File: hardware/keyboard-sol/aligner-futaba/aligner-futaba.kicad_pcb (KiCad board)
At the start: 2 copper layers, 386.1 x 117.7 mm, 96 parts, among them SW10 TAB: 1.25x, SW11 I, SW12 2, SW13 Zero, SW14 Q, SW15 O, SW16 3, SW17 Dash, SW18 W, SW19 P, SW20 4, SW21 Caret, SW22 E, SW23 AT, SW24 5, SW25 LT Bracket, SW26 R, SW27 Return: 1.5x, SW28 6, SW29 Backslash, SW30 T, SW31 Line Feed, SW32 7, SW33 RT Bracket, SW34 Y, SW35 Load, SW36 LT Ctrl, SW37 J, SW38 Upper Case: 1.5x, SW39 M, SW4 ESC: 1.75x, SW40 Shift Lock: 1.5x, SW41 K, SW42 LT Shift: 1.5x, SW43 Comma, SW44 A, SW45 L, SW46 Z, SW47 Period, SW48 S, SW49 Semicolon, SW5 8, SW50 X, SW51 Slash, SW52 D, SW53 Colon, SW54 C, SW55 RT Shift: 2x, SW56 F, SW57 DEL, SW58 V, SW59 Mode Select: 1.75x, SW6 BREAK, SW60 G, SW61 Repeat: 1.25x, SW62 B, SW63 H, SW64 RT Ctrl, SW65 N, SW66 Local, SW67 NP Dash, SW68 NP 4, SW69 NP Zero, SW7 U, SW70 Up Arrow, SW71 NP 7, SW72 NP 1, SW73 NP period, SW74 LT Arrow, SW75 NP asterisk, SW76 NP 5, SW77 NP plus, SW78 Spacebar, SW79 NP 8, SW8 1, SW80 NP 2, SW81 RT Arrow, SW82 NP divide, SW83 NP 6, SW84 Down Arrow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

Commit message: Moved mounting slots from keyboard PCB to aligners
- This allows the PCB to sink below the mounting brackets.  The aligner height can
be adjusted relative to the mounting brackets using spacers.

- changed futaba aligners to use cherry stabilizers.

- bumped rev number
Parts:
- removed the REF** at (318.1, 206.8)
- removed the REF** at (184.8, 206.8)
- SW55: footprint unikbd:Futaba-MD-4PCS-aligner -> unikbd:Futaba_2u_Cherry_aligner
- SW78: footprint unikbd:Futaba-MD-4PCS-aligner -> unikbd:Futaba_space_Cherry_aligner
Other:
- board size 386.1 x 117.7 mm -> 428.6 x 117.7 mm
- board text added: "SOL-20 Futaba MD-4PCS aligner Rev 1.1"
- board text removed: "SOL-20 Futaba MD-4PCS aligner Rev 1.0"

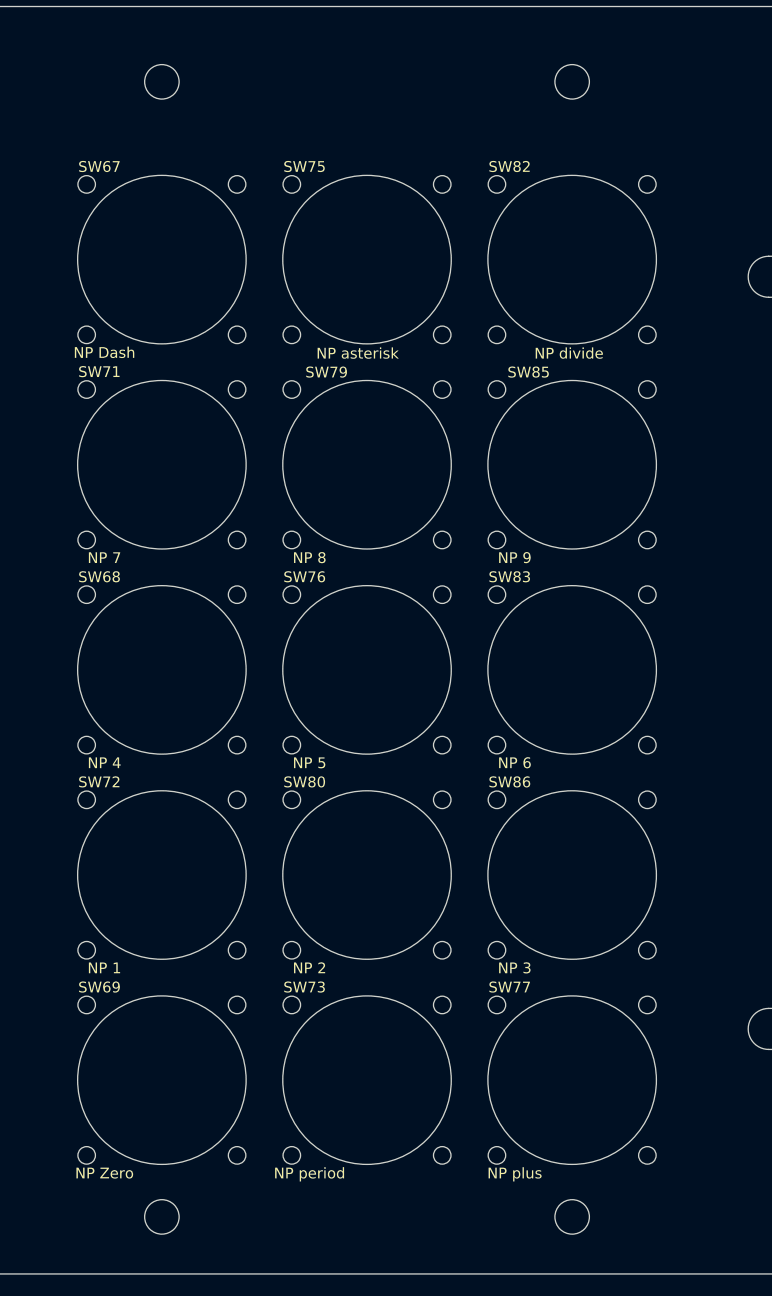
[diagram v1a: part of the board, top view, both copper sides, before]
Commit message: On aligners, moved numpad 0.1825" to the right.
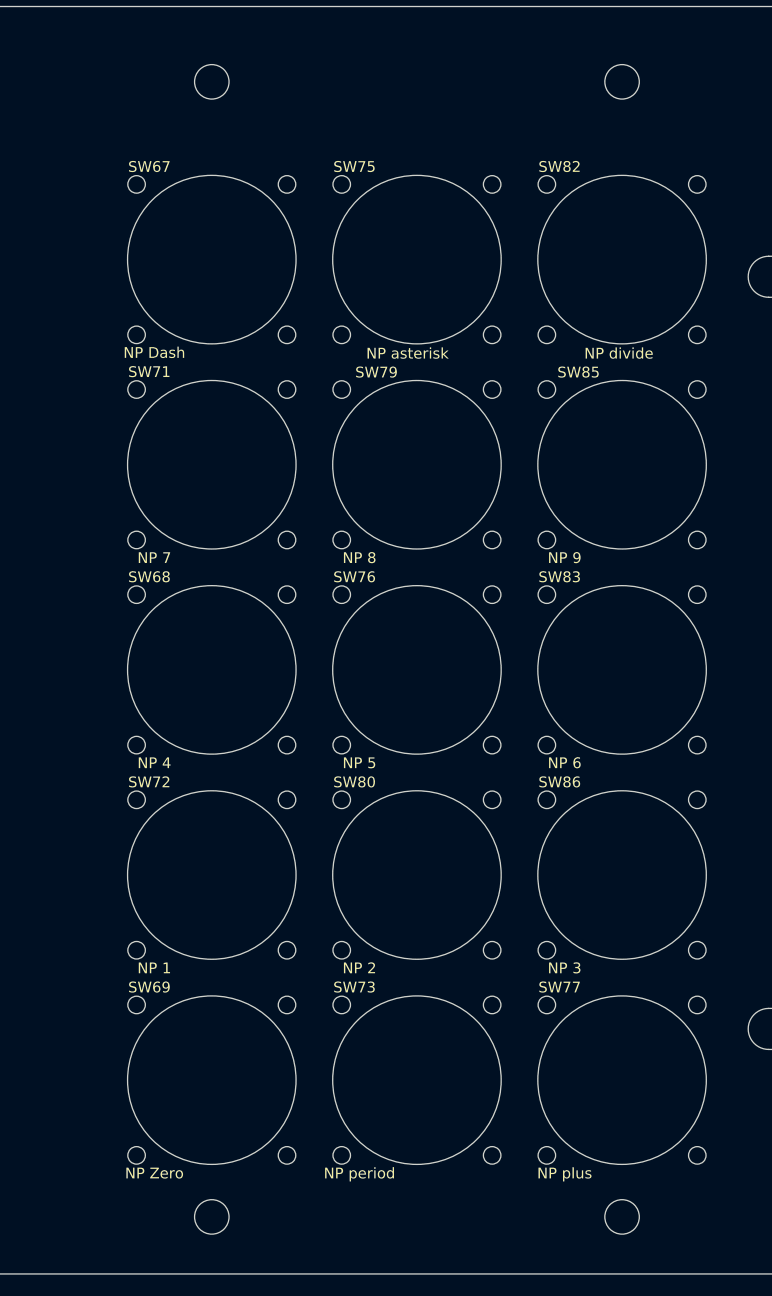
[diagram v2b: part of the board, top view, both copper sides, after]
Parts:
- removed the REF** at (432.4, 219.5)
- removed the REF** at (470.5, 219.5)
- removed the REF** at (470.5, 114.1)
- removed the REF** at (432.4, 114.1)
- added REF**: MountingHole_3.2mm_M3, MountingHole:MountingHole_3.2mm_M3, F.Cu at (437.1, 219.5)
- added REF**: MountingHole_3.2mm_M3, MountingHole:MountingHole_3.2mm_M3, F.Cu at (475.2, 219.5)
- added REF**: MountingHole_3.2mm_M3, MountingHole:MountingHole_3.2mm_M3, F.Cu at (475.2, 114.1)
- added REF**: MountingHole_3.2mm_M3, MountingHole:MountingHole_3.2mm_M3, F.Cu at (437.1, 114.1)
- moved SW73 4.64 mm to (456.1, 206.8)
- moved SW75 4.64 mm to (456.1, 130.6)
- moved SW76 4.64 mm to (456.1, 168.7)
- moved SW79 4.64 mm to (456.1, 149.6)
- moved SW80 4.64 mm to (456.1, 187.7)
- moved SW67 4.64 mm to (437.1, 130.6)
- moved SW68 4.64 mm to (437.1, 168.7)
- moved SW69 4.64 mm to (437.1, 206.8)
- moved SW71 4.64 mm to (437.1, 149.6)
- moved SW72 4.64 mm to (437.1, 187.7)
- moved SW77 4.64 mm to (475.2, 206.8)
- moved SW82 4.64 mm to (475.2, 130.6)
- moved SW83 4.64 mm to (475.2, 168.7)
- moved SW85 4.64 mm to (475.2, 149.6)
- moved SW86 4.64 mm to (475.2, 187.7)
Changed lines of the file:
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@@
   )
   (module unikbd:Futaba-MD-4PCS-aligner locked (layer F.Cu)
-    (at 451.47738 168.69156)
+    (at 456.11288 168.69156)
     (fp_text reference SW76 (at -5.7912 -8.6106) (layer F.SilkS)
       (effects (font (size 1 1) (thickness 0.15)))
@@
   )
   (module unikbd:Futaba-MD-4PCS-aligner locked (layer F.Cu)
-    (at 432.42738 168.69156)
+    (at 437.06288 168.69156)
     (fp_text reference SW68 (at -5.7912 -8.6106) (layer F.SilkS)
       (effects (font (size 1 1) (thickness 0.15)))
@@
   )
   (module unikbd:Futaba-MD-4PCS-aligner locked (layer F.Cu)
-    (at 470.52738 168.69156)
+    (at 475.16288 168.69156)
     (fp_text reference SW83 (at -5.7912 -8.6106) (layer F.SilkS)
       (effects (font (size 1 1) (thickness 0.15)))
@@
   )
   (module unikbd:Futaba-MD-4PCS-aligner locked (layer F.Cu)
-    (at 470.52738 149.64156)
+    (at 475.16288 149.64156)
     (fp_text reference SW85 (at -4.03098 -8.56996) (layer F.SilkS)
       (effects (font (size 1 1) (thickness 0.15)))
@@
   )
   (module unikbd:Futaba-MD-4PCS-aligner locked (layer F.Cu)
-    (at 470.52738 187.74156)
+    (at 475.16288 187.74156)
     (fp_text reference SW86 (at -5.7912 -8.6106) (layer F.SilkS)
       (effects (font (size 1 1) (thickness 0.15)))
@@
   )
   (module unikbd:Futaba-MD-4PCS-aligner locked (layer F.Cu)
-    (at 470.52738 130.59156)
+    (at 475.16288 130.59156)
     (fp_text reference SW82 (at -5.7912 -8.6106) (layer F.SilkS)
       (effects (font (size 1 1) (thickness 0.15)))
@@
   )
   (module unikbd:Futaba-MD-4PCS-aligner locked (layer F.Cu)
-    (at 451.47738 187.74156)
+    (at 456.11288 187.74156)
     (fp_text reference SW80 (at -5.7912 -8.6106) (layer F.SilkS)
       (effects (font (size 1 1) (thickness 0.15)))
@@
   )
   (module unikbd:Futaba-MD-4PCS-aligner locked (layer F.Cu)
-    (at 451.47738 149.64156)
+    (at 456.11288 149.64156)
     (fp_text reference SW79 (at -3.75158 -8.56996) (layer F.SilkS)
       (effects (font (size 1 1) (thickness 0.15)))
@@
   )
   (module unikbd:Futaba-MD-4PCS-aligner locked (layer F.Cu)
-    (at 470.52738 206.79156)
+    (at 475.16288 206.79156)
     (fp_text reference SW77 (at -5.7912 -8.6106) (layer F.SilkS)
       (effects (font (size 1 1) (thickness 0.15)))
@@
   )
   (module unikbd:Futaba-MD-4PCS-aligner locked (layer F.Cu)
-    (at 451.47738 130.59156)
+    (at 456.11288 130.59156)
     (fp_text reference SW75 (at -5.7912 -8.6106) (layer F.SilkS)
       (effects (font (size 1 1) (thickness 0.15)))
@@
   )
   (module unikbd:Futaba-MD-4PCS-aligner locked (layer F.Cu)
-    (at 451.47738 206.79156)
+    (at 456.11288 206.79156)
     (fp_text reference SW73 (at -5.7912 -8.6106) (layer F.SilkS)
       (effects (font (size 1 1) (thickness 0.15)))
@@
   )
   (module unikbd:Futaba-MD-4PCS-aligner locked (layer F.Cu)
-    (at 432.42738 187.74156)
+    (at 437.06288 187.74156)
     (fp_text reference SW72 (at -5.7912 -8.6106) (layer F.SilkS)
       (effects (font (size 1 1) (thickness 0.15)))
@@
   )
   (module unikbd:Futaba-MD-4PCS-aligner locked (layer F.Cu)
-    (at 432.42738 149.64156)
+    (at 437.06288 149.64156)
     (fp_text reference SW71 (at -5.7912 -8.6106) (layer F.SilkS)
       (effects (font (size 1 1) (thickness 0.15)))
@@
   )
   (module unikbd:Futaba-MD-4PCS-aligner locked (layer F.Cu)
-    (at 432.42738 206.79156)
+    (at 437.06288 206.79156)
     (fp_text reference SW69 (at -5.7912 -8.6106) (layer F.SilkS)
       (effects (font (size 1 1) (thickness 0.15)))
@@
   )
   (module unikbd:Futaba-MD-4PCS-aligner locked (layer F.Cu)
-    (at 432.42738 130.59156)
+    (at 437.06288 130.59156)
     (fp_text reference SW67 (at -5.7912 -8.6106) (layer F.SilkS)
       (effects (font (size 1 1) (thickness 0.15)))
@@
   )
   (module MountingHole:MountingHole_3.2mm_M3 locked (layer F.Cu)
-    (at 432.42738 219.49156)
+    (at 437.06288 219.49156)
     (descr "Mounting Hole 3.2mm, no annular, M3")
     (tags "mounting hole 3.2mm no annular m3")
@@
   )
   (module MountingHole:MountingHole_3.2mm_M3 locked (layer F.Cu)
-    (at 470.52738 219.49156)
+    (at 475.16288 219.49156)
     (descr "Mounting Hole 3.2mm, no annular, M3")
     (tags "mounting hole 3.2mm no annular m3")
@@
   )
   (module MountingHole:MountingHole_3.2mm_M3 locked (layer F.Cu)
-    (at 470.52738 114.08156)
+    (at 475.16288 114.08156)
     (descr "Mounting Hole 3.2mm, no annular, M3")
     (tags "mounting hole 3.2mm no annular m3")
@@
   )
   (module MountingHole:MountingHole_3.2mm_M3 locked (layer F.Cu)
-    (at 432.42738 114.08156)
+    (at 437.06288 114.08156)
     (descr "Mounting Hole 3.2mm, no annular, M3")
     (tags "mounting hole 3.2mm no annular m3")

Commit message: Adjsut mounting slots and alignment of mounting holes.
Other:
- outline, holes or cut-outs redrawn
- board text added: "SOL-20 Futaba MD-4PCS aligner Rev 1.4"
- board text removed: "SOL-20 Futaba MD-4PCS aligner Rev 1.1"
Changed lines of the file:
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@@
   (gr_circle (center 102.16388 187.74156) (end 105.38968 187.74156) (layer Edge.Cuts) (width 0.12))
   (gr_circle (center 121.21388 168.69156) (end 124.43968 168.69156) (layer Edge.Cuts) (width 0.12))
-  (gr_text "SOL-20 Futaba MD-4PCS aligner  Rev 1.1\n" (at 140.9954 112.7506) (layer F.SilkS)
+  (gr_text "SOL-20 Futaba MD-4PCS aligner  Rev 1.4\n" (at 140.9954 112.7506) (layer F.SilkS)
     (effects (font (size 2.032 2.032) (thickness 0.2032)) (justify left))
   )
@@
     (effects (font (size 2.032 2.032) (thickness 0.3048)) (justify left))
   )
-  (gr_line (start 505.45238 107.0864) (end 505.45238 130.27914) (layer Edge.Cuts) (width 0.1016))
-  (gr_line (start 505.45238 200.12914) (end 505.45238 134.08914) (layer Edge.Cuts) (width 0.1016))
-  (gr_line (start 505.45238 224.79) (end 505.45238 203.93914) (layer Edge.Cuts) (width 0.1016))
-  (gr_line (start 488.78109 203.93914) (end 505.44984 203.93914) (layer Edge.Cuts) (width 0.1016))
-  (gr_line (start 488.78109 134.08914) (end 505.44984 134.08914) (layer Edge.Cuts) (width 0.1016))
-  (gr_line (start 488.78109 130.27914) (end 505.44984 130.27914) (layer Edge.Cuts) (width 0.1016))
-  (gr_arc (start 488.78109 132.18414) (end 488.78109 130.27914) (angle -180) (layer Edge.Cuts) (width 0.1016))
-  (gr_line (start 488.78109 200.12914) (end 505.44984 200.12914) (layer Edge.Cuts) (width 0.1016))
-  (gr_arc (start 488.78109 202.03414) (end 488.78109 200.12914) (angle -180) (layer Edge.Cuts) (width 0.1016))
-  (gr_line (start 76.82738 134.08914) (end 76.82738 200.12914) (layer Edge.Cuts) (width 0.1016))
-  (gr_line (start 76.82738 107.0864) (end 76.82738 130.27914) (layer Edge.Cuts) (width 0.1016))
-  (gr_line (start 93.49613 130.27914) (end 76.82738 130.27914) (layer Edge.Cuts) (width 0.1016))
-  (gr_line (start 93.49613 134.08914) (end 76.82738 134.08914) (layer Edge.Cuts) (width 0.1016))
-  (gr_arc (start 93.49613 132.18414) (end 93.49613 130.27914) (angle 180) (layer Edge.Cuts) (width 0.1016))
-  (gr_line (start 93.49613 203.93914) (end 76.82738 203.93914) (layer Edge.Cuts) (width 0.1016))
-  (gr_line (start 93.49613 200.12914) (end 76.82738 200.12914) (layer Edge.Cuts) (width 0.1016))
-  (gr_line (start 76.82738 224.79) (end 76.82738 203.93914) (layer Edge.Cuts) (width 0.1016))
-  (gr_arc (start 93.49613 202.03414) (end 93.49613 200.12914) (angle 180) (layer Edge.Cuts) (width 0.1016))
+  (gr_line (start 505.45238 107.0864) (end 505.45238 132.81914) (layer Edge.Cuts) (width 0.1016))
+  (gr_line (start 505.45238 202.66914) (end 505.45238 136.62914) (layer Edge.Cuts) (width 0.1016))
+  (gr_line (start 505.45238 224.79) (end 505.45238 206.47914) (layer Edge.Cuts) (width 0.1016))
+  (gr_line (start 488.78109 206.47914) (end 505.44984 206.47914) (layer Edge.Cuts) (width 0.1016))
+  (gr_line (start 488.78109 136.62914) (end 505.44984 136.62914) (layer Edge.Cuts) (width 0.1016))
+  (gr_line (start 488.78109 132.81914) (end 505.44984 132.81914) (layer Edge.Cuts) (width 0.1016))
+  (gr_arc (start 488.78109 134.72414) (end 488.78109 132.81914) (angle -180) (layer Edge.Cuts) (width 0.1016))
+  (gr_line (start 488.78109 202.66914) (end 505.44984 202.66914) (layer Edge.Cuts) (width 0.1016))
+  (gr_arc (start 488.78109 204.57414) (end 488.78109 202.66914) (angle -180) (layer Edge.Cuts) (width 0.1016))
+  (gr_line (start 76.82738 136.62914) (end 76.82738 202.66914) (layer Edge.Cuts) (width 0.1016))
+  (gr_line (start 76.82738 107.0864) (end 76.82738 132.81914) (layer Edge.Cuts) (width 0.1016))
+  (gr_line (start 93.49613 132.81914) (end 76.82738 132.81914) (layer Edge.Cuts) (width 0.1016))
+  (gr_line (start 93.49613 136.62914) (end 76.82738 136.62914) (layer Edge.Cuts) (width 0.1016))
+  (gr_arc (start 93.49613 134.72414) (end 93.49613 132.81914) (angle 180) (layer Edge.Cuts) (width 0.1016))
+  (gr_line (start 93.49613 206.47914) (end 76.82738 206.47914) (layer Edge.Cuts) (width 0.1016))
+  (gr_line (start 93.49613 202.66914) (end 76.82738 202.66914) (layer Edge.Cuts) (width 0.1016))
+  (gr_line (start 76.82738 224.79) (end 76.82738 206.47914) (layer Edge.Cuts) (width 0.1016))
+  (gr_arc (start 93.49613 204.57414) (end 93.49613 202.66914) (angle 180) (layer Edge.Cuts) (width 0.1016))
   (gr_line (start 76.82738 224.79) (end 505.45238 224.79) (layer Edge.Cuts) (width 0.1))
   (gr_line (start 505.45238 107.0864) (end 76.82738 107.0864) (layer Edge.Cuts) (width 0.1016))

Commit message: Added stabilizer bending guide and futaba stabilizer posts to PCB
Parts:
- added REF**: Rod sizing hole 1/16 inch, MountingHole:MountingHole_3.2mm_M3, F.Cu at (184.8, 220.9)
- added REF**: Rod sizing hole 1/16 inch, MountingHole:MountingHole_3.2mm_M3, F.Cu at (318.1, 220.9)
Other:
- outline, holes or cut-outs redrawn
- board text added: "File to 1.5mm"
- board text added: "Post Thickness Gauge"
- board text added: "SOL-20 Futaba MD-4PCS aligner Rev 1.5"
- board text added: "Stabilizer bar bending guide holes"
- board text added: "Unified Keyboard Project."
- board text added: "https://github.com/osiweb/unified_retro_keyboard"
- board text removed: "SOL-20 Futaba MD-4PCS aligner Rev 1.4"
- board text removed: "Unified Keyboard Project. https://github.com/osiweb/unified_retro_keyboard"

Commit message: Tiny adjustment to stabilizer post width gauge
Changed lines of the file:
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@@
     (pad 1 np_thru_hole circle (at 0 0) (size 3.2 3.2) (drill 3.2) (layers *.Cu *.Mask))
+  )
+  (gr_text "File to\n1.5mm" (at 378.40666 115.49634 180) (layer F.SilkS)
+    (effects (font (size 1 1) (thickness 0.15)))
   )
   (gr_line (start 373.59808 117.54022) (end 383.75808 117.54022) (layer Edge.Cuts) (width 0.1016))
@@
   (gr_line (start 355.75808 117.54022) (end 355.75808 113.52784) (layer Edge.Cuts) (width 0.1016))
   (gr_line (start 385.34512 110.35224) (end 354.17058 110.35284) (layer Edge.Cuts) (width 0.1016))
-  (gr_text "File to\n1.5mm" (at 378.40666 115.49634 180) (layer F.SilkS)
+  (gr_text "File to\n1.5mm" (at 299.01134 115.40998 180) (layer F.SilkS)
     (effects (font (size 1 1) (thickness 0.15)))
   )
@@
   (gr_line (start 276.36058 117.45468) (end 284.52318 117.45468) (layer Edge.Cuts) (width 0.1016))
   (gr_arc (start 274.77526 111.85398) (end 274.77526 110.26648) (angle -90) (layer Edge.Cuts) (width 0.1016))
-  (gr_text "File to\n1.5mm" (at 299.01134 115.40998 180) (layer F.SilkS)
-    (effects (font (size 1 1) (thickness 0.15)))
-  )
   (gr_arc (start 81.60198 151.01652) (end 81.60198 149.42902) (angle -90) (layer Edge.Cuts) (width 0.1016))
   (gr_line (start 80.01448 151.01652) (end 80.01508 182.19106) (layer Edge.Cuts) (width 0.1016))
@@
     (effects (font (size 1 1) (thickness 0.15)) (justify left))
   )
-  (gr_line (start 505.45238 107.0864) (end 223.14154 107.0864) (layer Edge.Cuts) (width 0.1016))
+  (gr_line (start 505.45238 107.0864) (end 223.090743 107.0864) (layer Edge.Cuts) (width 0.1016))
   (gr_line (start 221.590743 112.4204) (end 221.590743 107.0864) (layer Edge.Cuts) (width 0.1016))
-  (gr_line (start 223.14154 112.4204) (end 223.14154 107.0864) (layer Edge.Cuts) (width 0.1016))
-  (gr_line (start 221.590743 112.4204) (end 223.14154 112.4204) (layer Edge.Cuts) (width 0.1016))
+  (gr_line (start 223.090743 112.4204) (end 223.090743 107.0864) (layer Edge.Cuts) (width 0.1016))
+  (gr_line (start 221.590743 112.4204) (end 223.090743 112.4204) (layer Edge.Cuts) (width 0.1016))
   (gr_line (start 187.50026 220.40596) (end 219.42552 218.36634) (layer F.SilkS) (width 0.12))
   (gr_line (start 277.27656 218.67368) (end 316.55258 220.69044) (layer F.SilkS) (width 0.12))
